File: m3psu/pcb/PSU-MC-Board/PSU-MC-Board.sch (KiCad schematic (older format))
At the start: 56 parts, among them IC1 STM32F405RxTx, IC2 TPS62152, IC3 MCP2562, IC4 LTC4353, IC5 LTC4151, J1 WEST TOP, J2 WEST BOT, J3 NORTH TOP, J4 EAST TOP, J5 EAST BOT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

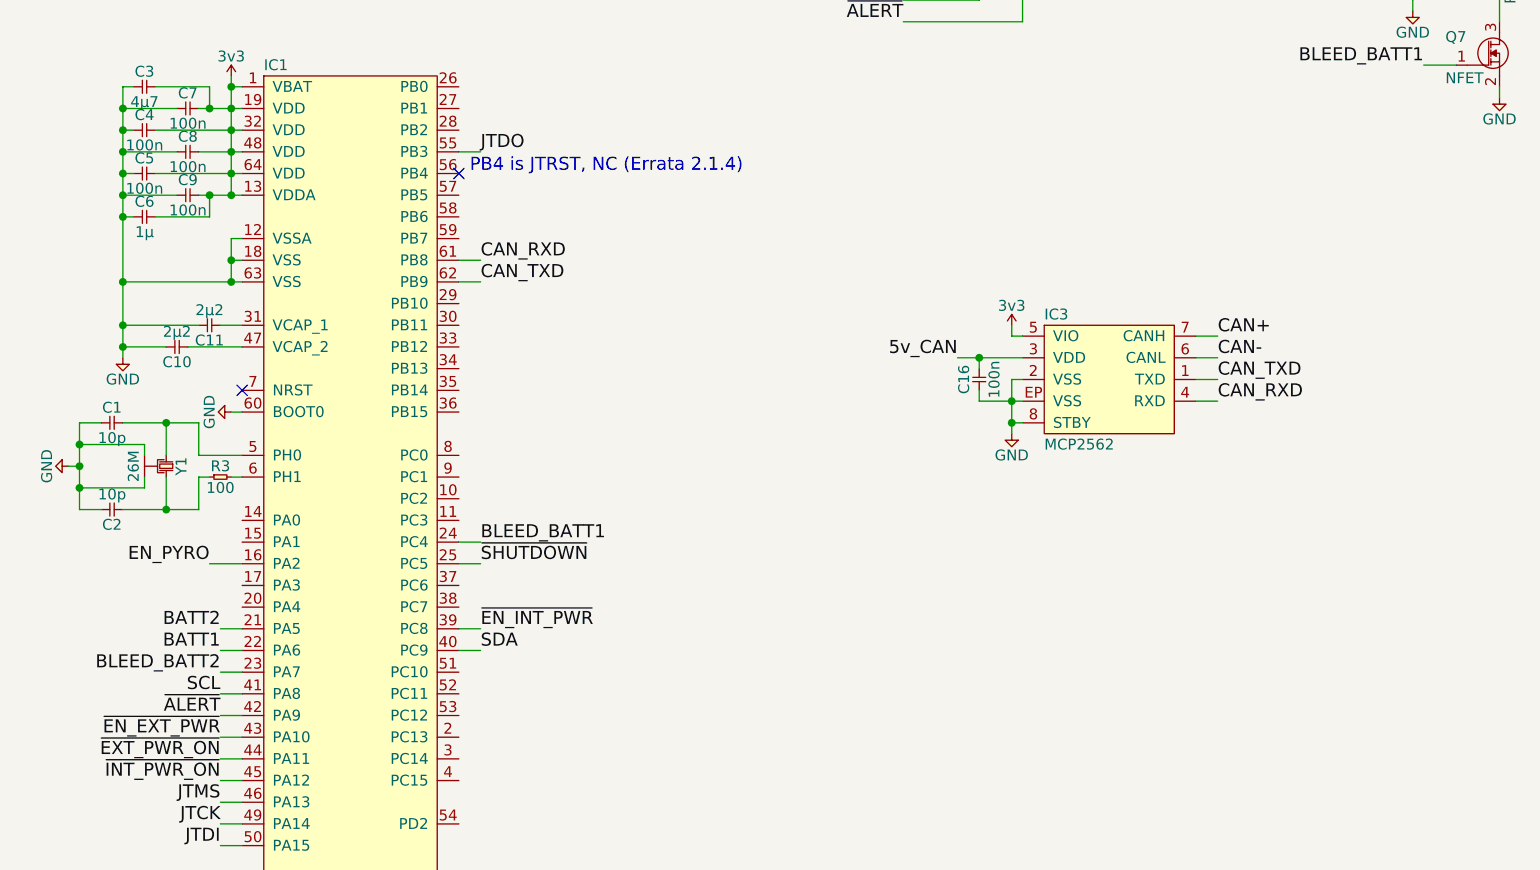
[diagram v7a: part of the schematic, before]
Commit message: Add voltage dividers to battery monitor lines
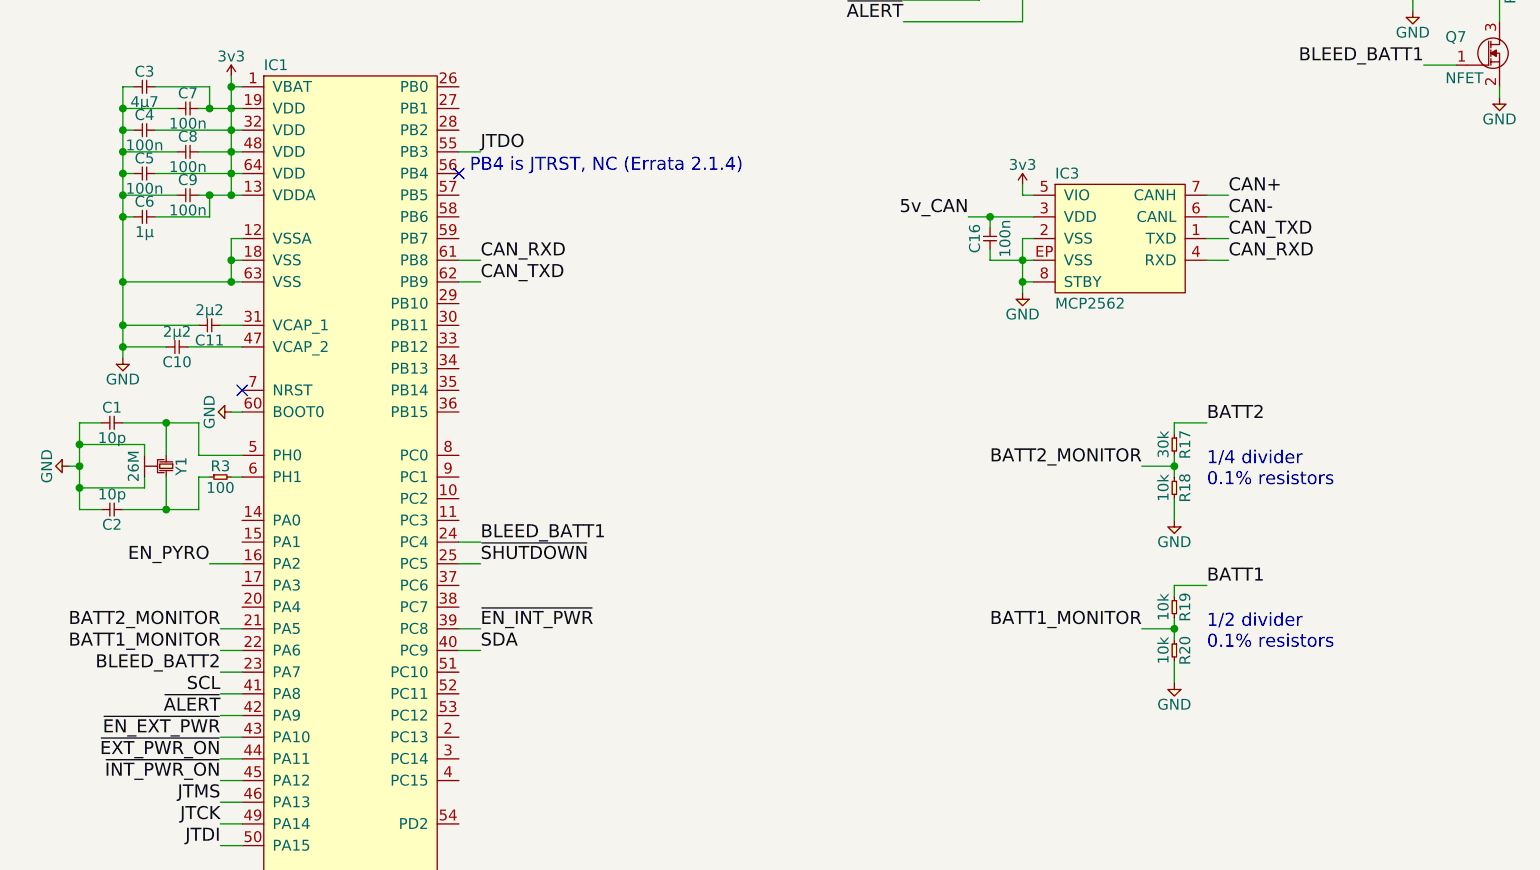
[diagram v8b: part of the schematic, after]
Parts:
- added R17: 30k, agg:0402, symbol R
- added R18, R19, R20: 10k, agg:0402, symbol R
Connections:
- net BATT1: now also R19.1; no longer IC1.22 (PA6)
- net BATT2: now also R17.1; no longer IC1.21 (PA5)
- net GND: now also R18.2, R20.2
- new net BATT1_MONITOR: IC1.22 (PA6), R19.2, R20.1
- new net BATT2_MONITOR: IC1.21 (PA5), R17.2, R18.1
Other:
- note added: "1/2 divider\n0.1% resistors"
- note added: "1/4 divider\n0.1% resistors"
- moved on the sheet: C16, IC3
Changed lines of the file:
@@
 L MCP2562 IC3
 U 1 1 56DF4FA9
-P 5450 5350
-F 0 "IC3" H 5150 5650 50  0000 L CNN
-F 1 "MCP2562" H 5150 5050 50  0000 L CNN
-F 2 "agg:DFN-8-EP-MICROCHIP" H 5150 4950 50  0001 L CNN
-F 3 "http://ww1.microchip.com/downloads/en/DeviceDoc/20005167C.pdf" H 5150 4850 50  0001 L CNN
-F 4 "" H 5150 4750 50  0001 L CNN "Farnell"
-F 5 "824-3135" H 5150 4650 50  0001 L CNN "RS"
-	1    5450 5350
+P 5500 4700
+F 0 "IC3" H 5200 5000 50  0000 L CNN
+F 1 "MCP2562" H 5200 4400 50  0000 L CNN
+F 2 "agg:DFN-8-EP-MICROCHIP" H 5200 4300 50  0001 L CNN
+F 3 "http://ww1.microchip.com/downloads/en/DeviceDoc/20005167C.pdf" H 5200 4200 50  0001 L CNN
+F 4 "" H 5200 4100 50  0001 L CNN "Farnell"
+F 5 "824-3135" H 5200 4000 50  0001 L CNN "RS"
+	1    5500 4700
 	1    0    0    -1
 $EndComp
@@
 L 3v3 #PWR05
 U 1 1 56E3BF2E
-P 5000 5100
-F 0 "#PWR05" H 5000 5210 50  0001 L CNN
-F 1 "3v3" H 5000 5190 50  0000 C CNN
-F 2 "" H 5000 5100 60  0000 C CNN
-F 3 "" H 5000 5100 60  0000 C CNN
-	1    5000 5100
+P 5050 4450
+F 0 "#PWR05" H 5050 4560 50  0001 L CNN
+F 1 "3v3" H 5050 4540 50  0000 C CNN
+F 2 "" H 5050 4450 60  0000 C CNN
+F 3 "" H 5050 4450 60  0000 C CNN
+	1    5050 4450
 	-1   0    0    -1
 $EndComp
@@
 L C C16
 U 1 1 56E4016F
-P 4850 5300
-F 0 "C16" H 4900 5370 50  0000 C CNN
-F 1 "100n" H 4900 5230 50  0000 C CNN
-F 2 "agg:0402" H 4850 5300 50  0001 C CNN
-F 3 "" H 4850 5300 50  0001 C CNN
-F 4 "2496771" H 4850 5300 60  0001 C CNN "Farnell"
-	1    4850 5300
+P 4900 4650
+F 0 "C16" H 4950 4720 50  0000 C CNN
+F 1 "100n" H 4950 4580 50  0000 C CNN
+F 2 "agg:0402" H 4900 4650 50  0001 C CNN
+F 3 "" H 4900 4650 50  0001 C CNN
+F 4 "2496771" H 4900 4650 60  0001 C CNN "Farnell"
+	1    4900 4650
 	0    -1   1    0
 $EndComp
@@
 L GND #PWR06
 U 1 1 56E40658
-P 5000 5600
-F 0 "#PWR06" H 4870 5640 50  0001 L CNN
-F 1 "GND" H 5000 5500 50  0000 C CNN
-F 2 "" H 5000 5600 60  0000 C CNN
-F 3 "" H 5000 5600 60  0000 C CNN
-	1    5000 5600
+P 5050 4950
+F 0 "#PWR06" H 4920 4990 50  0001 L CNN
+F 1 "GND" H 5050 4850 50  0000 C CNN
+F 2 "" H 5050 4950 60  0000 C CNN
+F 3 "" H 5050 4950 60  0000 C CNN
+	1    5050 4950
 	-1   0    0    -1
 $EndComp
@@
 Text Label 2550 4800 0    60   ~ 0
 CAN_RXD
-Text Label 5950 5350 0    60   ~ 0
+Text Label 6000 4700 0    60   ~ 0
 CAN_TXD
-Text Label 5950 5450 0    60   ~ 0
+Text Label 6000 4800 0    60   ~ 0
 CAN_RXD
-Text Label 4750 5250 2    60   ~ 0
+Text Label 4800 4600 2    60   ~ 0
 5v_CAN
 Text Label 1350 7300 2    60   ~ 0
@@
 Text Label 1350 7500 2    60   ~ 0
 JTDI
-Text Label 5950 5150 0    60   ~ 0
+Text Label 6000 4500 0    60   ~ 0
 CAN+
-Text Label 5950 5250 0    60   ~ 0
+Text Label 6000 4600 0    60   ~ 0
 CAN-
 Text Label 7450 2850 0    60   ~ 0
@@
 	1250 5700 1450 5700
 Wire Wire Line
-	5950 5150 5850 5150
-Wire Wire Line
-	5950 5250 5850 5250
-Wire Wire Line
-	5000 5100 5000 5150
-Wire Wire Line
-	5000 5150 5050 5150
-Wire Wire Line
-	4750 5250 5050 5250
-Wire Wire Line
-	4850 5250 4850 5300
-Connection ~ 4850 5250
-Wire Wire Line
-	5050 5350 5000 5350
-Wire Wire Line
-	5000 5350 5000 5600
-Wire Wire Line
-	5050 5550 5000 5550
-Connection ~ 5000 5550
-Wire Wire Line
-	4850 5450 5050 5450
-Connection ~ 5000 5450
-Wire Wire Line
-	4850 5450 4850 5400
+	6000 4500 5900 4500
+Wire Wire Line
+	6000 4600 5900 4600
+Wire Wire Line
+	5050 4450 5050 4500
+Wire Wire Line
+	5050 4500 5100 4500
+Wire Wire Line
+	4800 4600 5100 4600
+Wire Wire Line
+	4900 4600 4900 4650
+Connection ~ 4900 4600
+Wire Wire Line
+	5100 4700 5050 4700
+Wire Wire Line
+	5050 4700 5050 4950
+Wire Wire Line
+	5100 4900 5050 4900
+Connection ~ 5050 4900
+Wire Wire Line
+	4900 4800 5100 4800
+Connection ~ 5050 4800
+Wire Wire Line
+	4900 4800 4900 4750
 Wire Wire Line
 	4850 3600 4850 3450
@@
 	2450 4800 2550 4800
 Wire Wire Line
-	5850 5350 5950 5350
-Wire Wire Line
-	5850 5450 5950 5450
+	5900 4700 6000 4700
+Wire Wire Line
+	5900 4800 6000 4800
 Wire Wire Line
 	1450 7300 1350 7300
@@
 Wire Wire Line
 	1350 6700 1450 6700
+Wire Wire Line
+	1350 6600 1450 6600
+Wire Wire Line
+	1350 6500 1450 6500
+Text Label 5900 6300 0    60   ~ 0
+BATT1
+Wire Wire Line
+	5900 6300 5750 6300
+Wire Wire Line
+	5750 6300 5750 6350
+Wire Wire Line
+	5750 6550 5750 6450
+Wire Wire Line
+	5750 6500 5600 6500
+Connection ~ 5750 6500
+Wire Wire Line
+	5750 6650 5750 6750
+$Comp
+L GND #PWR050
+U 1 1 57280704
+P 5750 6750
+F 0 "#PWR050" H 5620 6790 50  0001 L CNN
+F 1 "GND" H 5750 6650 50  0000 C CNN
+F 2 "" H 5750 6750 60  0000 C CNN
+F 3 "" H 5750 6750 60  0000 C CNN
+	1    5750 6750
+	-1   0    0    -1
+$EndComp
+$Comp
+L R R20
+U 1 1 57284D3D
+P 5750 6550
+F 0 "R20" H 5800 6600 50  0000 C CNN
+F 1 "10k" H 5800 6500 50  0000 C CNN
+F 2 "agg:0402" H 5750 6550 50  0001 C CNN
+F 3 "" H 5750 6550 50  0001 C CNN
+F 4 "1577717" H 5750 6550 60  0001 C CNN "Farnell"
+	1    5750 6550
+	0    1    1    0
+$EndComp
 Text Label 1350 6600 2    60   ~ 0
-BATT1
-Wire Wire Line
-	1350 6600 1450 6600
+BATT1_MONITOR
+Text Label 5600 6500 2    60   ~ 0
+BATT1_MONITOR
+Text Label 5900 5550 0    60   ~ 0
+BATT2
+Wire Wire Line
+	5900 5550 5750 5550
+Wire Wire Line
+	5750 5550 5750 5600
+Wire Wire Line
+	5750 5800 5750 5700
+Wire Wire Line
+	5750 5750 5600 5750
+Connection ~ 5750 5750
+Wire Wire Line
+	5750 5900 5750 6000
+$Comp
+L GND #PWR051
+U 1 1 572862EC
+P 5750 6000
+F 0 "#PWR051" H 5620 6040 50  0001 L CNN
+F 1 "GND" H 5750 5900 50  0000 C CNN
+F 2 "" H 5750 6000 60  0000 C CNN
+F 3 "" H 5750 6000 60  0000 C CNN
+	1    5750 6000
+	-1   0    0    -1
+$EndComp
+$Comp
+L R R17
+U 1 1 572862F3
+P 5750 5600
+F 0 "R17" H 5800 5650 50  0000 C CNN
+F 1 "30k" H 5800 5550 50  0000 C CNN
+F 2 "agg:0402" H 5750 5600 50  0001 C CNN
+F 3 "" H 5750 5600 50  0001 C CNN
+F 4 "2324779" H 5750 5600 60  0001 C CNN "Farnell"
+	1    5750 5600
+	0    1    1    0
+$EndComp
+$Comp
+L R R18
+U 1 1 572862FB
+P 5750 5800
+F 0 "R18" H 5800 5850 50  0000 C CNN
+F 1 "10k" H 5800 5750 50  0000 C CNN
+F 2 "agg:0402" H 5750 5800 50  0001 C CNN
+F 3 "" H 5750 5800 50  0001 C CNN
+F 4 "1577717" H 5750 5800 60  0001 C CNN "Farnell"
+	1    5750 5800
+	0    1    1    0
+$EndComp
+Text Label 5600 5750 2    60   ~ 0
+BATT2_MONITOR
 Text Label 1350 6500 2    60   ~ 0
-BATT2
-Wire Wire Line
-	1350 6500 1450 6500
+BATT2_MONITOR
+$Comp
+L R R19
+U 1 1 5728C34B
+P 5750 6350
+F 0 "R19" H 5800 6400 50  0000 C CNN
+F 1 "10k" H 5800 6300 50  0000 C CNN
+F 2 "agg:0402" H 5750 6350 50  0001 C CNN
+F 3 "" H 5750 6350 50  0001 C CNN
+F 4 "1577717" H 5750 6350 60  0001 C CNN "Farnell"
+	1    5750 6350
+	0    1    1    0
+$EndComp
+Text Notes 5900 5850 0    60   ~ 0
+1/4 divider\n0.1% resistors
+Text Notes 5900 6600 0    60   ~ 0
+1/2 divider\n0.1% resistors
 $EndSCHEMATC
